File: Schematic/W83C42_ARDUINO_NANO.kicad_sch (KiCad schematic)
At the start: 23 parts, among them J2 Mini-DIN-6, J3 DIN-5, U1 74HC14, Y1 Crystal

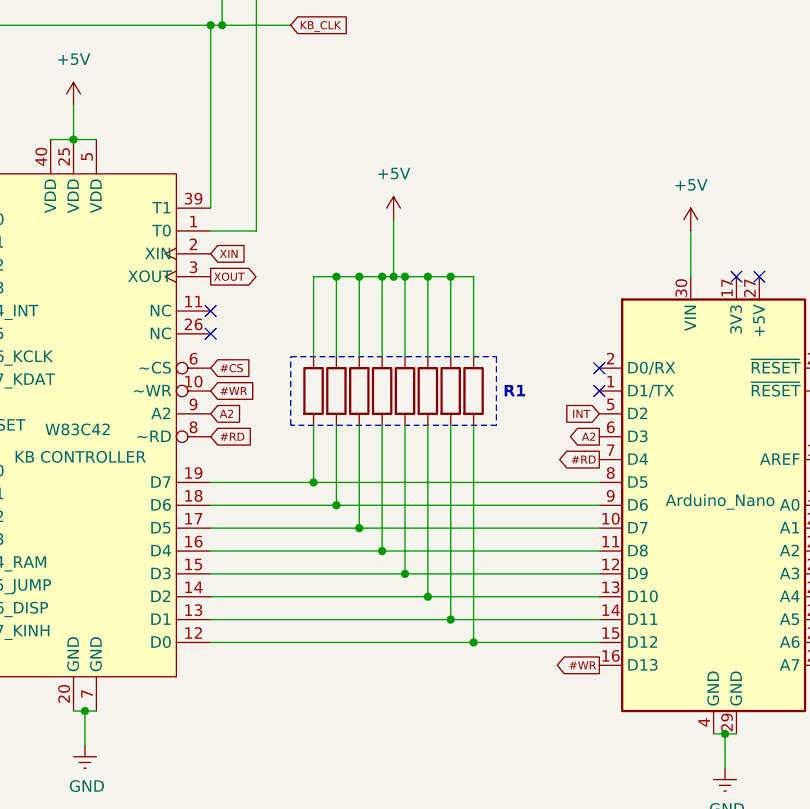
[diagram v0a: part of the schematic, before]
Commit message: Removed unnecessary pullup resistors from the data lines, the resistors were there to make sure that the data bus is always in a known state, but are no longer needed since any reading of the bus done by the processor or the W83C42 is done safely. Updated the schematic and the photo of the schematic.
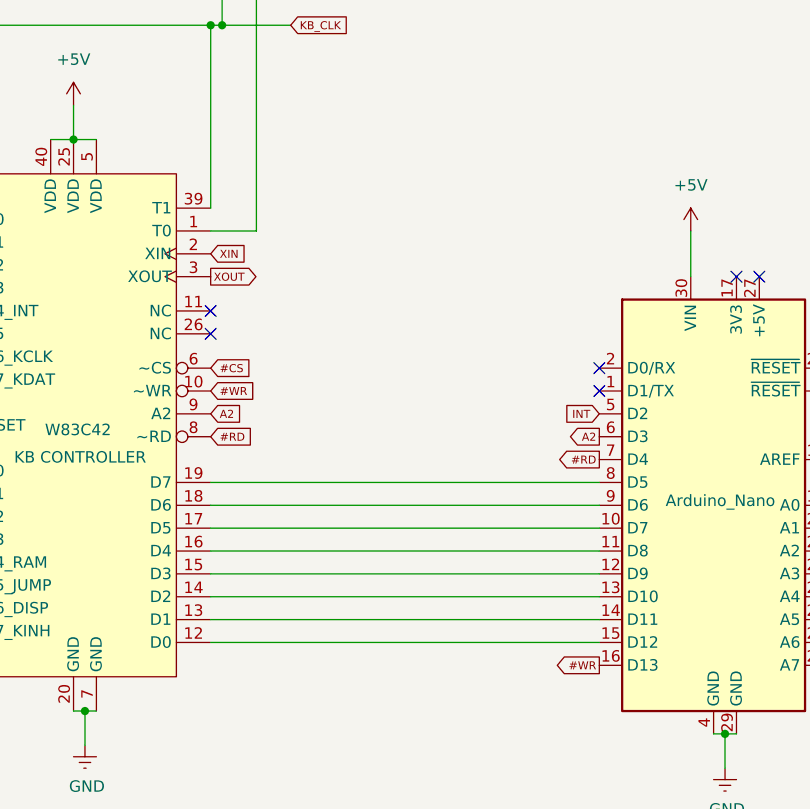
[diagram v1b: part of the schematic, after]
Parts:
- removed R1, R2, R3, R4, R5, R6, R7, R8: R, symbol Device:R
